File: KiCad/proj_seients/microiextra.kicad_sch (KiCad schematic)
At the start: 58 parts, among them J10 Screw_Terminal_01x05, J11 PushButton, J12 PushButton, J13 PushButton, J14 PushButton, J15 PushButton, J16 PushButton, J17 PushButton, J18 PushButton, J2 5f0857756ylz, J3 DE-9, J8 DE9_Socket, J9 PushButton, SW1 SW_Push, U1 PIC24HJ128GP502, U10 MAX3232, U4 TCAN1043xDxQ1, U9 24LC256, Y1 8MHz

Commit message: Canvi de TCAN i Afegit CAN DE.9
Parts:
- removed C26, C27: 100nF, symbol Device:C
- removed C28: 10uF, symbol Device:C_Polarized_US
- removed J3: DE-9, symbol Connector:Screw_Terminal_01x02
- removed R3: 10k, symbol Device:R
- removed U4: TCAN1043xDxQ1, Package_SO:SOIC-14_3.9x8.7mm_P1.27mm, symbol Interface_CAN_LIN:TCAN1043xDxQ1
- added J19: DE9_Socket, Connector_Dsub:DSUB-9_Socket_Vertical_P2.77x2.84mm, symbol Connector:DE9_Socket
- added U4: MCP2562-E-SN, Package_SO:SOIC-8_3.9x4.9mm_P1.27mm, symbol Interface_CAN_LIN:MCP2562-E-SN
- R2: value 10k -> 120
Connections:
- net 3.3V: now also U4.5 (Vio); no longer R2.2
- net 5V: now also U4.3 (VDD)
- net CAN_RX: now also U4.4 (RXD)
- net CAN_TX: now also U4.1 (TXD)
- net GND: now also J19.3, U4.2 (VSS), U4.8 (STBY)
- net CAN_L: now reaches R2.1
- net CAN_L: now also J19.2, U4.6 (CANL)
- new net CAN_H: J19.7, R2.2, U4.7 (CANH)
- no-connect marks 13 -> 17
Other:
- note added: "Autors: Miguel Tovar i Pol Salas Etapa relacionada amb el microcontrolador i altres funcionaments"
- note added: "Conector CAN DE-9"
- note added: "Hebilla sensor integrado"
- note removed: "Autors: Miguel Tovar i Pol Salas"
- note removed: "Hebilla comercial con sensor integrado"
- moved on the sheet: J2, J8

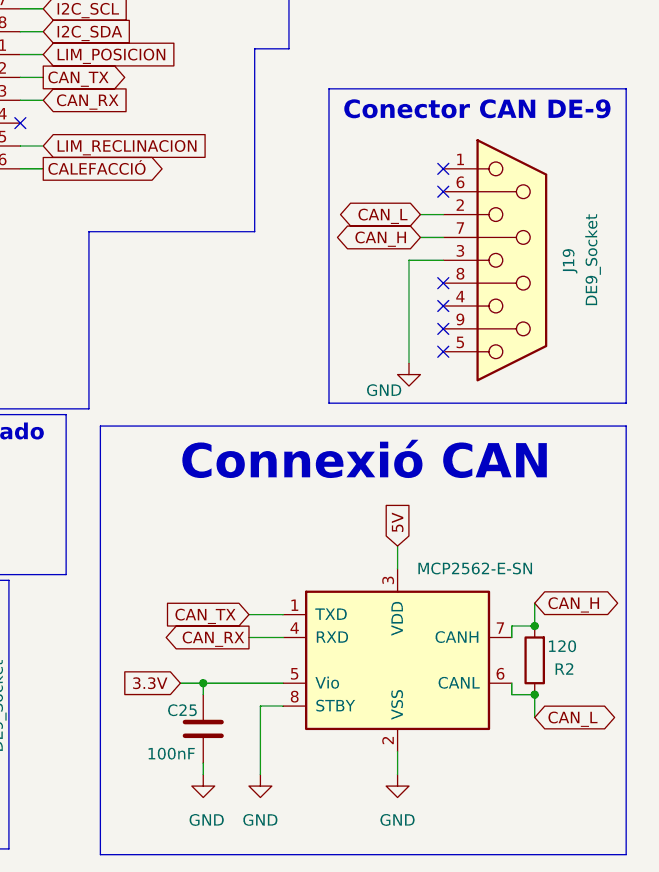
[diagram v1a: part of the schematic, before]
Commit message: Afegit C protecció als 5V del CAN
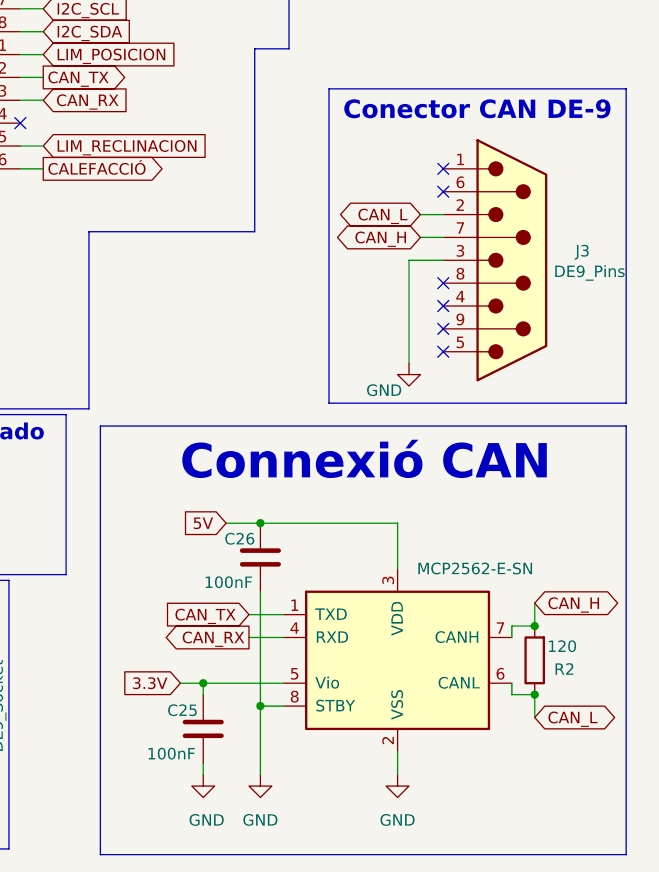
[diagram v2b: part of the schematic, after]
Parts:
- removed J19: DE9_Socket, Connector_Dsub:DSUB-9_Socket_Vertical_P2.77x2.84mm, symbol Connector:DE9_Socket
- added C26: 100nF, symbol Device:C
- added J3: DE9_Pins, symbol Connector:DE9_Pins
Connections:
- net 5V: now also C26.2
- net CAN_H: now also J3.7
- net CAN_L: now also J3.2
- net GND: now also C26.1, J3.3
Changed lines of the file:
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@@
 	)
 	(junction
+		(at 242.57 128.27)
+		(diameter 0)
+		(color 0 0 0 0)
+	)
+	(junction
 		(at 72.39 64.77)
 		(diameter 0)
@@
 	)
 	(junction
+		(at 242.57 148.59)
+		(diameter 0)
+		(color 0 0 0 0)
+	)
+	(junction
 		(at 69.85 157.48)
 		(diameter 0)
@@
 	(wire
 		(pts
+			(xy 242.57 128.27) (xy 257.81 128.27)
+		)
+		(stroke
+			(width 0)
+			(type default)
+		)
+	)
+	(wire
+		(pts
 			(xy 273.05 137.16) (xy 273.05 139.7)
 		)
@@
 	(wire
 		(pts
+			(xy 238.76 128.27) (xy 242.57 128.27)
+		)
+		(stroke
+			(width 0)
+			(type default)
+		)
+	)
+	(wire
+		(pts
 			(xy 124.46 36.83) (xy 127 36.83)
 		)
@@
 	(wire
 		(pts
+			(xy 242.57 135.89) (xy 242.57 148.59)
+		)
+		(stroke
+			(width 0)
+			(type default)
+		)
+	)
+	(wire
+		(pts
 			(xy 124.46 34.29) (xy 127 34.29)
 		)
@@
 		)
 	)
+	(wire
+		(pts
+			(xy 257.81 128.27) (xy 257.81 133.35)
+		)
+		(stroke
+			(width 0)
+			(type default)
+		)
+	)
 	(polyline
 		(pts
@@
 		)
 	)
-	(wire
-		(pts
-			(xy 257.81 130.81) (xy 257.81 133.35)
-		)
-		(stroke
-			(width 0)
-			(type default)
-		)
-	)
 	(polyline
 		(pts
@@
 	(global_label "5V"
 		(shape input)
-		(at 257.81 130.81 90)
+		(at 238.76 128.27 180)
 		(fields_autoplaced yes)
 		(effects
@@
 				(size 1.27 1.27)
 			)
-			(justify left)
+			(justify right)
 		)
 		(property "Intersheetrefs" "${INTERSHEET_REFS}"
-			(at 257.81 125.5267 90)
+			(at 233.4767 128.27 0)
 			(effects
 				(font
 					(size 1.27 1.27)
 				)
-				(justify left)
+				(justify right)
 				(hide yes)
 			)
@@
 	)
 	(symbol
-		(lib_id "Connector:DE9_Socket")
-		(at 270.51 99.06 0)
-		(unit 1)
-		(exclude_from_sim no)
-		(in_bom yes)
-		(on_board yes)
-		(dnp no)
-		(fields_autoplaced yes)
-		(property "Reference" "J19"
-			(at 276.86 99.06 90)
-			(effects
-				(font
-					(size 1.27 1.27)
-				)
-			)
-		)
-		(property "Value" "DE9_Socket"
-			(at 279.4 99.06 90)
-			(effects
-				(font
-					(size 1.27 1.27)
-				)
-			)
-		)
-		(property "Footprint" "Connector_Dsub:DSUB-9_Socket_Vertical_P2.77x2.84mm"
-			(at 270.51 99.06 0)
-			(effects
-				(font
-					(size 1.27 1.27)
-				)
-				(hide yes)
-			)
-		)
-		(property "Datasheet" "~"
-			(at 270.51 99.06 0)
-			(effects
-				(font
-					(size 1.27 1.27)
-				)
-				(hide yes)
-			)
-		)
-		(property "Description" "9-pin D-SUB connector, socket (female)"
-			(at 270.51 99.06 0)
-			(effects
-				(font
-					(size 1.27 1.27)
-				)
-				(hide yes)
-			)
-		)
-		(pin "6"
-		)
-		(pin "8"
-		)
-		(pin "7"
-		)
-		(pin "5"
-		)
-		(pin "9"
-		)
-		(pin "1"
-		)
-		(pin "2"
-		)
-		(pin "4"
-		)
-		(pin "3"
-		)
-		(instances
-			(project "proj_seients"
-				(path "/abdea21b-3040-408b-b009-221f8b614884/4b7a2b31-c07e-4668-81d2-c9fcd52362f2"
-					(reference "J19")
-					(unit 1)
-				)
-			)
-		)
-	)
-	(symbol
 		(lib_id "power:GND")
 		(at 242.57 39.37 0)
@@
 	)
 	(symbol
+		(lib_id "Device:C")
+		(at 242.57 132.08 180)
+		(unit 1)
+		(exclude_from_sim no)
+		(in_bom yes)
+		(on_board yes)
+		(dnp no)
+		(property "Reference" "C26"
+			(at 240.284 130.048 0)
+			(effects
+				(font
+					(size 1.27 1.27)
+				)
+			)
+		)
+		(property "Value" "100nF"
+			(at 239.014 134.874 0)
+			(effects
+				(font
+					(size 1.27 1.27)
+				)
+			)
+		)
+		(property "Footprint" ""
+			(at 241.6048 128.27 0)
+			(effects
+				(font
+					(size 1.27 1.27)
+				)
+				(hide yes)
+			)
+		)
+		(property "Datasheet" "~"
+			(at 242.57 132.08 0)
+			(effects
+				(font
+					(size 1.27 1.27)
+				)
+				(hide yes)
+			)
+		)
+		(property "Description" "Unpolarized capacitor"
+			(at 242.57 132.08 0)
+			(effects
+				(font
+					(size 1.27 1.27)
+				)
+				(hide yes)
+			)
+		)
+		(pin "1"
+		)
+		(pin "2"
+		)
+		(instances
+			(project "proj_seients"
+				(path "/abdea21b-3040-408b-b009-221f8b614884/4b7a2b31-c07e-4668-81d2-c9fcd52362f2"
+					(reference "C26")
+					(unit 1)
+				)
+			)
+		)
+	)
+	(symbol
 		(lib_id "power:GND")
 		(at 257.81 156.21 0)
@@
 					(unit 1)
 				)
+			)
+		)
+	)
+	(symbol
+		(lib_id "Connector:DE9_Pins")
+		(at 270.51 99.06 0)
+		(mirror x)
+		(unit 1)
+		(exclude_from_sim no)
+		(in_bom yes)
+		(on_board yes)
+		(dnp no)
+		(property "Reference" "J3"
+			(at 278.384 98.044 0)
+			(effects
+				(font
+					(size 1.27 1.27)
+				)
+			)
+		)
+		(property "Value" "DE9_Pins"
+			(at 279.146 100.33 0)
+			(effects
+				(font
+					(size 1.27 1.27)
+				)
+			)
+		)
+		(property "Footprint" ""
+			(at 270.51 99.06 0)
+			(effects
+				(font
+					(size 1.27 1.27)
+				)
+				(hide yes)
+			)
+		)
+		(property "Datasheet" "~"
+			(at 270.51 99.06 0)
+			(effects
+				(font
+					(size 1.27 1.27)
+				)
+				(hide yes)
+			)
+		)
+		(property "Description" "9-pin D-SUB connector, pins (male)"
+			(at 270.51 99.06 0)
+			(effects
+				(font
+					(size 1.27 1.27)
+				)
+				(hide yes)
+			)
+		)
+		(pin "8"
+		)
+		(pin "7"
+		)
+		(pin "1"
+		)
+		(pin "5"
+		)
+		(pin "3"
+		)
+		(pin "6"
+		)
+		(pin "9"
+		)
+		(pin "2"
+		)
+		(pin "4"
+		)
+		(instances
+			(project ""
+				(path "/abdea21b-3040-408b-b009-221f8b614884/4b7a2b31-c07e-4668-81d2-c9fcd52362f2"
+					(reference "J3")
+					(unit 1)
+				)

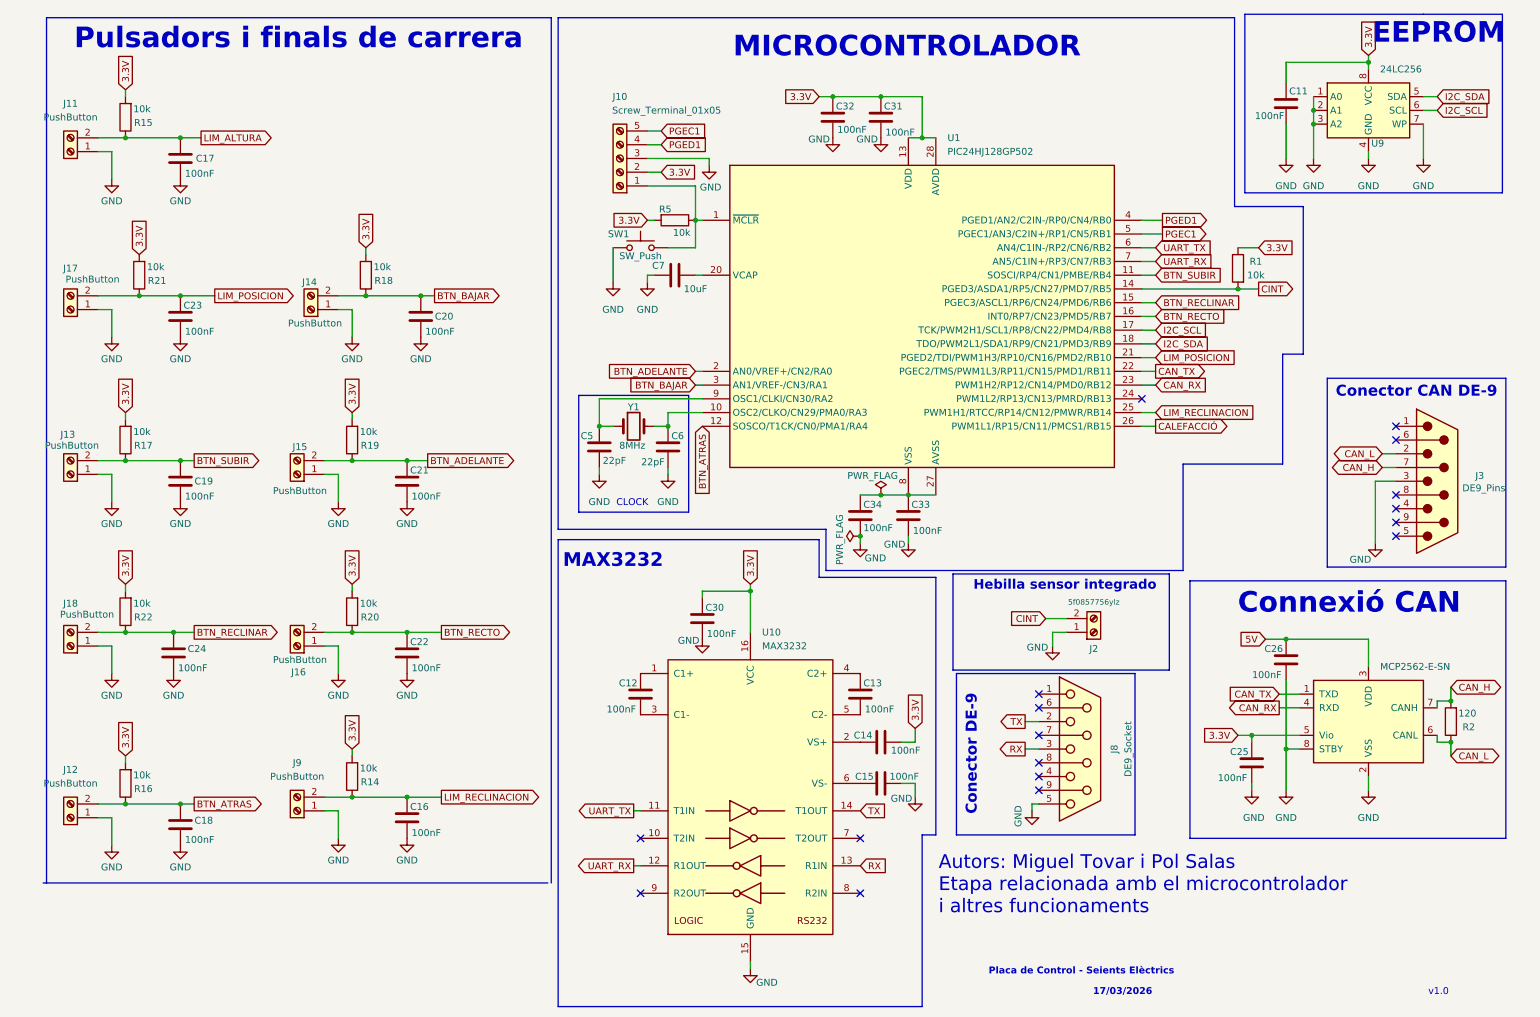
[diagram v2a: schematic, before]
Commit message: Canvis de pulsadors, estètica dels drivers i commentaris extres
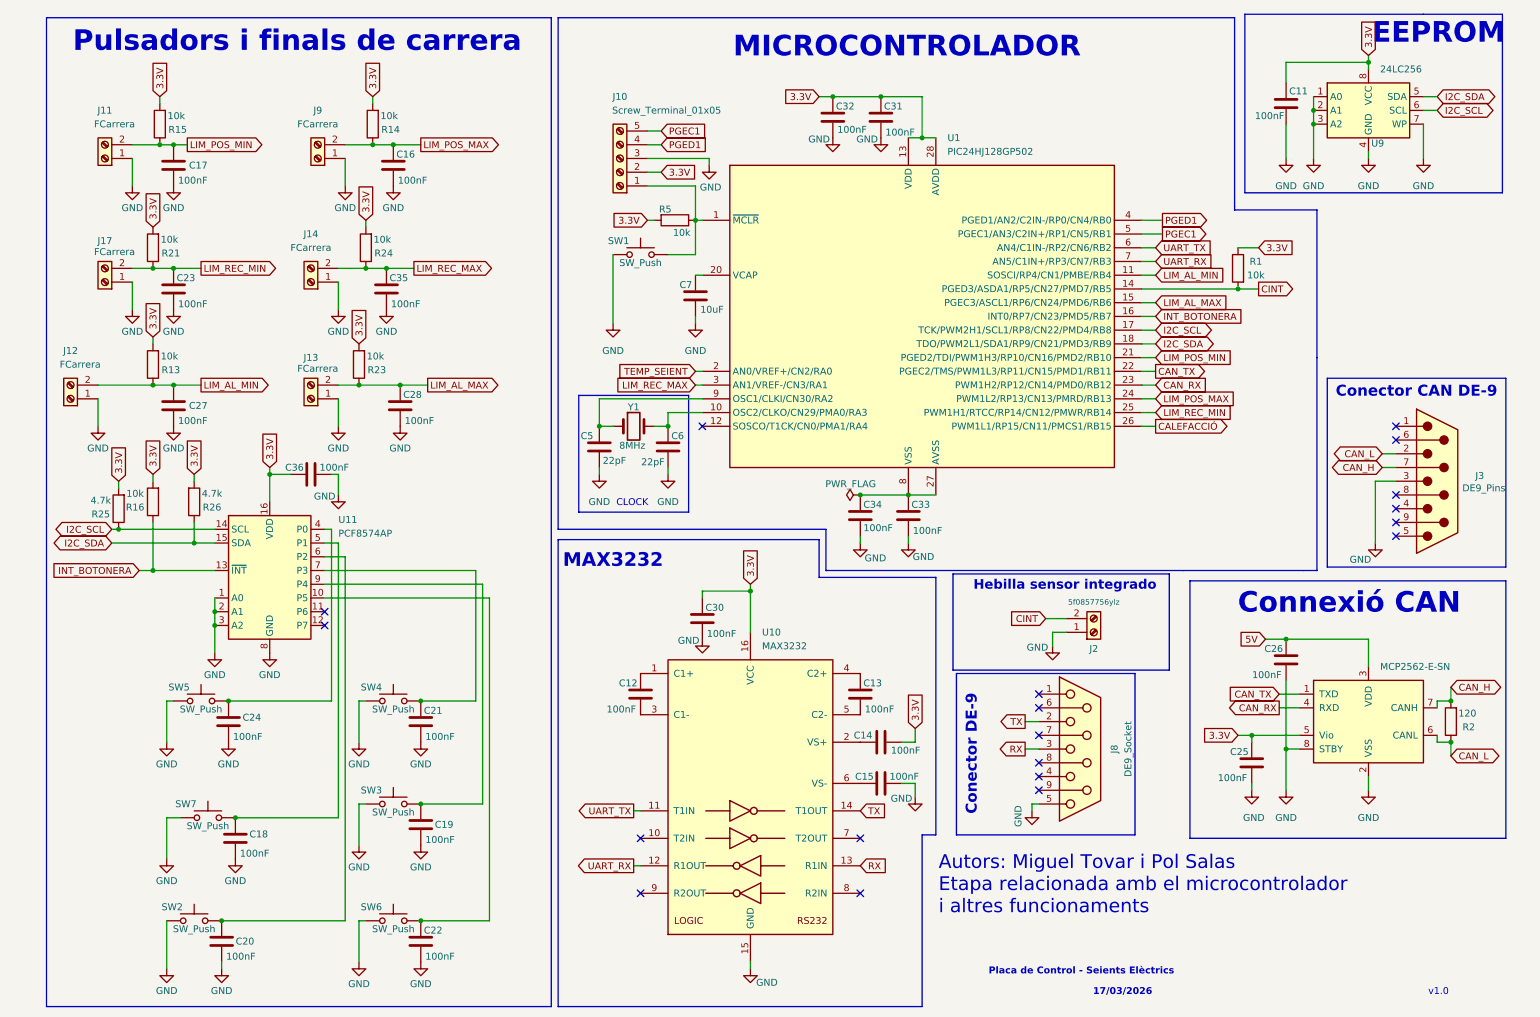
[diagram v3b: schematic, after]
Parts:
- removed J15, J16, J18: PushButton, symbol Connector:Screw_Terminal_01x02
- removed R17, R18, R19, R20, R22: 10k, symbol Device:R
- added C27, C28, C35, C36: 100nF, symbol Device:C
- added R13, R23, R24: 10k, symbol Device:R
- added R25, R26: 4.7k, symbol Device:R
- added SW2, SW3, SW4, SW5, SW6, SW7: SW_Push, symbol Switch:SW_Push
- added U11: PCF8574AP, Package_DIP:DIP-16_W7.62mm, symbol Interface_Expansion:PCF8574AP
- J11, J12, J13, J14, J17, J9: value PushButton -> FCarrera
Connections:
- net 3.3V: now also C36.2, R13.2, R23.2, R24.2, R25.2, R26.2, U11.16 (VDD)
- net GND: now also C27.1, C28.1, C35.1, C36.1, SW2.1, SW3.1, SW4.1, SW5.1, SW6.1, SW7.1, U11.1 (A0), U11.2 (A1), U11.3 (A2), U11.8 (GND)
- net I2C_SCL: now also R25.1, U11.14 (SCL)
- net I2C_SDA: now also R26.1, U11.15 (SDA)
- net LIM_POS_MAX: now reaches U1.24 (PWM1L2/RP13/CN13/PMRD/RB13)
- net LIM_POS_MAX: now also C16.2, J9.2 (Pin_2), R14.1
- net BTN_ADELANTE: no longer names the net of C21.2
- net BTN_ADELANTE: now also SW4.2, U11.7 (P3); no longer U1.2 (AN0/VREF+/CN2/RA0)
- removed net BTN_ATRAS: C18.2, J12.2 (Pin_2), R16.1, U1.12 (SOSCO/T1CK/CN0/PMA1/RA4)
- net BTN_BAJAR renamed LIM_REC_MAX
- net LIM_REC_MAX: now also C35.2, R24.1; no longer C20.2
- net BTN_RECLINAR: no longer names the net of C24.2
- net BTN_RECLINAR: now also SW5.2, U11.4 (P0); no longer U1.15 (PGEC3/ASCL1/RP6/CN24/PMD6/RB6)
- net BTN_RECTO: no longer names the net of C22.2
- net BTN_RECTO: now also SW6.2, U11.10 (P5); no longer U1.16 (INT0/RP7/CN23/PMD5/RB7)
- removed net BTN_SUBIR: C19.2, J13.2 (Pin_2), U1.11 (SOSCI/RP4/CN1/PMBE/RB4)
- net LIM_ALTURA renamed LIM_POS_MIN
- net LIM_POS_MIN: now also U1.21 (PGED2/TDI/PWM1H3/RP10/CN16/PMD2/RB10)
- net LIM_POSICION renamed LIM_REC_MIN
- net LIM_REC_MIN: now also U1.25 (PWM1H1/RTCC/RP14/CN12/PMWR/RB14); no longer U1.21 (PGED2/TDI/PWM1H3/RP10/CN16/PMD2/RB10)
- removed net LIM_RECLINACION: C16.2, J9.2 (Pin_2), R14.1, U1.25 (PWM1H1/RTCC/RP14/CN12/PMWR/RB14)
- new net: C18.2, SW7.2, U11.5 (P1)
- new net: C19.2, SW3.2, U11.9 (P4)
- new net: C20.2, SW2.2, U11.6 (P2)
- new net INT_BOTONERA: R16.1, U1.16 (INT0/RP7/CN23/PMD5/RB7), U11.13 (~{INT})
- new net LIM_AL_MAX: C28.2, J13.2 (Pin_2), R23.1, U1.15 (PGEC3/ASCL1/RP6/CN24/PMD6/RB6)
- new net LIM_AL_MIN: C27.2, J12.2 (Pin_2), R13.1, U1.11 (SOSCI/RP4/CN1/PMBE/RB4)
- new net TEMP_SEIENT: U1.2 (AN0/VREF+/CN2/RA0)
- no-connect marks 17 -> 19
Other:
- moved on the sheet: C16, C17, C18, C19, C20, C21, C22, C23, C24, C7, J11, J17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
